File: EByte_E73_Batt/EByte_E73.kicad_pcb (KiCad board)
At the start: 2 copper layers, 21.6 x 62.2 mm, 14 parts, among them J1 USB_OTG, J2 Serial Connector, U1 E73-2G4M04S, U2 ProMicro, U3 AP2112K-3.3, U4 CP2102N-A01-GQFN24, U5 MCP73831-2-OT

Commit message: completed V2.0
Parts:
- removed U5: MCP73831-2-OT, TO_SOT_Packages_SMD:SOT-23-5_HandSoldering
- added C5: 10uF, Capacitors_SMD:C_0805_HandSoldering, F.Cu at (114.4, 137.3)
- added C6: 1nF, Capacitors_SMD:C_0805_HandSoldering, B.Cu at (111.4, 103.4)
- added C7: 10uF, Capacitors_SMD:C_0805_HandSoldering, F.Cu at (111.0, 134.2)
- added C8: 10uF, Capacitors_SMD:C_0805_HandSoldering, F.Cu at (112.3, 144.4)
- added C9: 0.1uF, Capacitors_SMD:C_0805_HandSoldering, F.Cu at (106.3, 142.4)
- added D1: MBR120, Diodes_SMD:D_SOD-123, F.Cu at (106.2, 139.4)
- added J3: Conn_01x02, Pin_Headers:Pin_Header_Straight_1x02_Pitch2.54mm, F.Cu at (106.1, 134.2)
- added JP1: JUMPER-SMT_2_NO, E73:SolderJumperSingle, F.Cu at (103.5, 148.3)
- added Q1: DMG3415U, TO_SOT_Packages_SMD:SOT-23, F.Cu at (111.0, 137.2)
- added R2: 100K, Resistors_SMD:R_0805_HandSoldering, F.Cu at (112.2, 142.3)
- added R3: 10K, Resistors_SMD:R_0805_HandSoldering, F.Cu at (111.0, 132.3)
- added R4: 806K, Resistors_SMD:R_0805_HandSoldering, B.Cu at (104.8, 103.8)
- added R5: 2M, Resistors_SMD:R_0805_HandSoldering, B.Cu at (111.5, 105.4)
- added R6: 1K, Resistors_SMD:R_0805_HandSoldering, F.Cu at (106.3, 144.4)
- added U6: TP4056, Power_Integrations:SO-8, B.Cu at (110.5, 135.4)
- C3, U3: moved to B.Cu
- U4: value CP2102N-A01-GQFN24 -> CH340C; footprint Housings_DFN_QFN:QFN-24-1EP_4x4mm_Pitch0.5mm -> SMD_Packages:SO-16-N; moved to B.Cu
- moved U3 29.9 mm to (105.4, 129.8), turned to 90 degrees
- moved C3 11.4 mm to (106.0, 114.5), turned to 90 degrees
- moved R1 10.6 mm to (108.3, 114.4), turned to 270 degrees
- moved J2 7.65 mm to (112.2, 129.7)
- moved C2 7.57 mm to (104.7, 108.9), turned to 0 degrees
- moved C1 5.08 mm to (104.8, 111.0), turned to 0 degrees
- moved C4 2.82 mm to (104.7, 106.9)
- moved L1 2.53 mm to (103.5, 114.5)
- moved U4 0.95 mm to (109.2, 143.7), turned to 180 degrees
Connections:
- J1 pad 1: (no net) -> /VBus
- J1 pad 2: (no net) -> /Data-
- J1 pad 3: (no net) -> /Data+
- J1 pad 5: (no net) -> GND
- R1 pad 1: (no net) -> RESET
- U1 pad 11: (no net) -> /P0.31
- U3 pad 1: (no net) -> Net-(C5-Pad1)
- U3 pad 2: (no net) -> GND
- U3 pad 3: (no net) -> Net-(C5-Pad1)
- U3 pad 5: (no net) -> VCC
- U4 pad 1: (no net) -> GND
- U4 pad 13: (no net) -> /DTR
- U4 pad 16: (no net) -> /VBus
- U4 pad 2: (no net) -> Net-(R6-Pad2)
- U4 pad 3: (no net) -> TXD
- U4 pad 4: (no net) -> /VBus
- U4 pad 5: (no net) -> /Data+
- U4 pad 6: (no net) -> /Data-
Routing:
- net GND: track 102.4 -> 198.8 mm, vias 11 -> 18
- net /VBatt: track 0.00 -> 48.5 mm, vias 0 -> 2
- net /VBus: track 0.00 -> 42.1 mm, vias 0 -> 3
- net TXD: track 18.9 -> 50.8 mm, vias 1 -> 3
- net Net-(C5-Pad1): track 0.00 -> 25.2 mm, vias 0 -> 1
- net /P0.31: track 0.00 -> 24.3 mm, vias 0 -> 1
- net /P0.07: track 18.6 -> 39.5 mm, vias 1 -> 2
- net RXD: track 19.3 -> 40.0 mm, vias 1 -> 0
- net /P0.17: track 24.1 -> 40.3 mm, vias 1 -> 0
- net Net-(J1-Pad6): track 0.00 -> 13.0 mm
- net SWDCLK: track 34.5 -> 22.9 mm
- net RESET: track 61.5 -> 72.3 mm
- net SWDIO: track 35.0 -> 24.6 mm
- net SCK: track 21.8 -> 29.9 mm
- net Net-(R3-Pad1): track 0.00 -> 6.70 mm, vias 0 -> 1
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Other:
- board text added: "+Batt"
- board text added: "Designed By /u/jpconstantineau"
- board text added: "For Assembly Instructions, refer to: https://github.com/jpconstantineau /NRF52-Board For Firmware, refer to: https://github.com/jpconstantineau /BlueMicro_BLE"
- board text added: "For use with NRF52832 Module"
- board text added: "Jump for DTR Reset"
- board text added: "LiPo Battery Charger"
- board text added: "P0.02"
- board text added: "P0.03"
- board text added: "P0.04"
- board text added: "P0.05"
- board text added: "P0.07"
- board text added: "P0.11"
- board text added: "P0.12"
- board text added: "P0.13"
- board text added: "P0.14"
- board text added: "P0.15"
- board text added: "P0.16"
- board text added: "P0.17"
- board text added: "P0.25"
- board text added: "P0.26"
- board text added: "P0.27"
- board text added: "P0.28"
- board text added: "P0.29"
- board text added: "P0.30"
- board text added: "SWDCK"
- board text added: "V2.0"
- board text removed: "SWDCLK"
- board text removed: "V1.1"

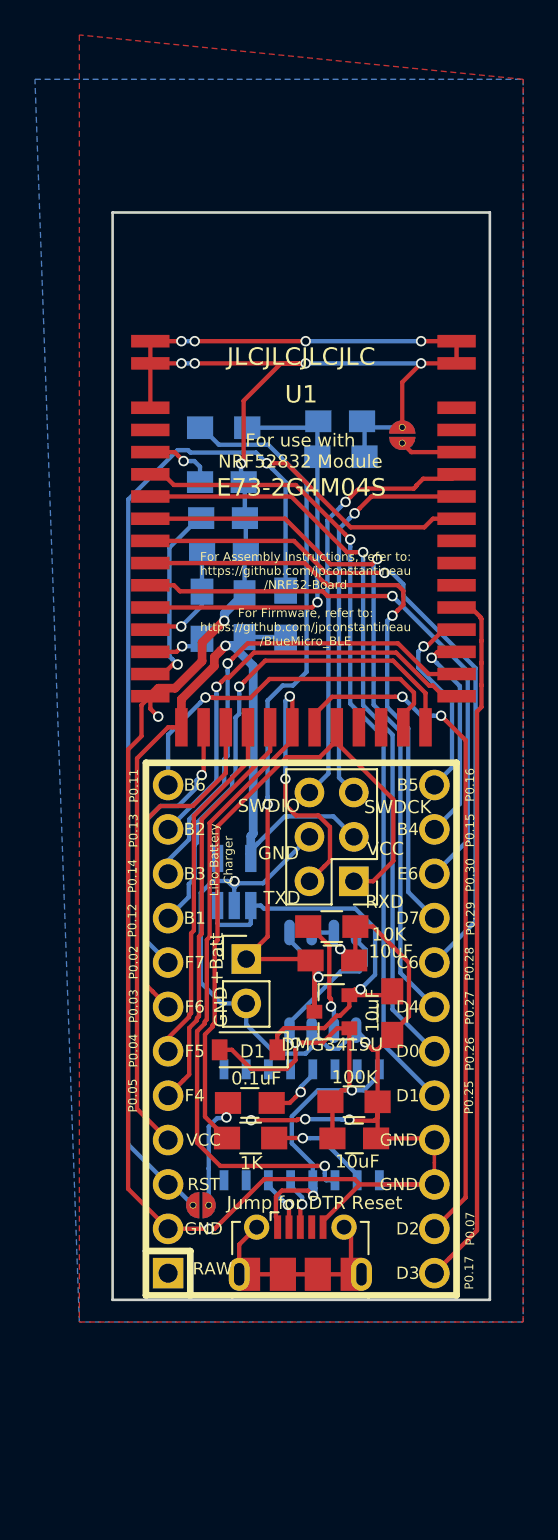
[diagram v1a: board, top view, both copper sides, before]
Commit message: adding battery switch PCB
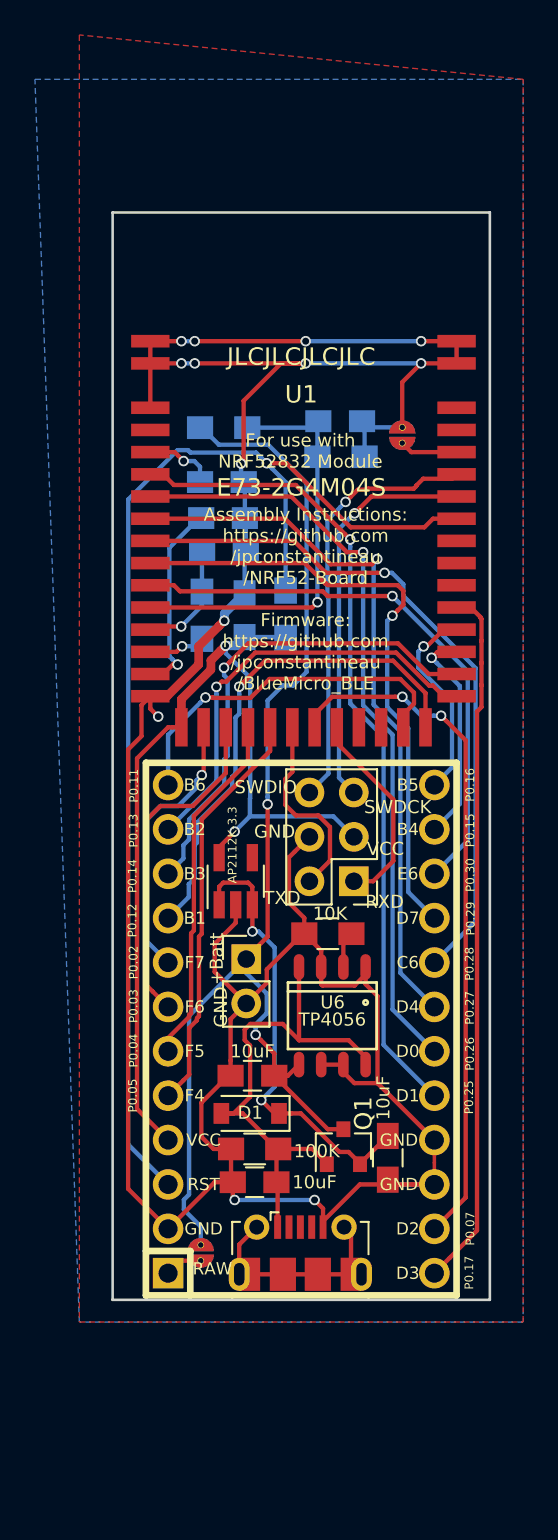
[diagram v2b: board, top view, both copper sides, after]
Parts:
- removed C9: 0.1uF, Capacitors_SMD:C_0805_HandSoldering
- removed JP1: JUMPER-SMT_2_NO, E73:SolderJumperSingle
- removed R6: 1K, Resistors_SMD:R_0805_HandSoldering
- removed U4: CH340C, SMD_Packages:SO-16-N
- added JP3: JUMPER-SMT_2_NO, E73:SolderJumperSingle, F.Cu at (103.5, 151.0)
- U3, U6: moved to F.Cu
- moved C5 8.28 mm to (114.2, 145.5)
- moved C7 8.03 mm to (106.4, 140.8), turned to 180 degrees
- moved Q1 7.75 mm to (111.6, 144.9), turned to 90 degrees
- moved R2 6.30 mm to (106.6, 145.0), turned to 180 degrees
- moved C8 6.23 mm to (106.6, 146.9), turned to 180 degrees
- moved D1 3.64 mm to (106.3, 143.0)
- moved U6 2.04 mm to (111.0, 137.4)
- moved R3 0.46 mm to (110.7, 132.7), turned to 180 degrees
- moved U3 0.10 mm to (105.5, 129.7)
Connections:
- J1 pad 2: /Data- -> (no net)
- J1 pad 3: /Data+ -> (no net)
- U2 pad 1: (no net) -> Net-(JP3-Pad2)
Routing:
- net TXD: track 50.8 -> 12.8 mm, vias 3 -> 0
- net RXD: track 40.0 -> 12.5 mm
- net /VBatt: track 48.5 -> 69.5 mm
- net GND: track 198.8 -> 187.5 mm, vias 18 -> 13
- net /VBus: track 42.1 -> 30.8 mm, vias 3 -> 0
- net Net-(C9-Pad1): track 6.60 -> 0.00 mm, vias 1 -> 0
- net Net-(R6-Pad2): track 5.94 -> 0.00 mm, vias 1 -> 0
- net Net-(R3-Pad1): track 6.70 -> 2.10 mm, vias 1 -> 0
- net /DTR: track 3.73 -> 0.00 mm, vias 1 -> 0
- net /Data-: track 3.19 -> 0.00 mm, vias 1 -> 0
- net /Data+: track 3.00 -> 0.00 mm, vias 1 -> 0
- net Net-(JP3-Pad2): track 0.00 -> 2.17 mm
- net RESET: track 72.3 -> 70.8 mm
- net VCC: track 57.6 -> 56.3 mm, vias 1 -> 2
- net Net-(C5-Pad1): track 25.2 -> 25.9 mm, vias 1 -> 2
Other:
- board text added: "Assembly Instructions: https://github.com /jpconstantineau /NRF52-Board Firmware: https://github.com /jpconstantineau /BlueMicro_BLE"
- board text added: "V2.0b"
- board text removed: "For Assembly Instructions, refer to: https://github.com/jpconstantineau /NRF52-Board For Firmware, refer to: https://github.com/jpconstantineau /BlueMicro_BLE"
- board text removed: "Jump for DTR Reset"
- board text removed: "V2.0"
